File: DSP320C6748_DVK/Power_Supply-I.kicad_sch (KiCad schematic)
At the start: 17 parts, among them IC1 TPS650250RHBR, IC2 TPS3707-33DR, IC3 TPS2087D, IC4 TPS2068DGNR, IC5 SN74AHC1G04DBVR, J1 Barrel_Jack_Switch, J2 USB_B_Mini, U2 NCP-347MTAE

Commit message: TPS650250 Section Added
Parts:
- removed IC1: TPS650250RHBR, TPS650250RHBR:QFN50P500X500X100-33N-D, symbol TPS650250RHBR:TPS650250RHBR
- added D2: PWR_Red, symbol Device:LED_Small
- added R7: 1K, symbol Device:R_Small
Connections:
- net +5V: now also R7.1
- net GND: now also D2.1 (K)
- new net: D2.2 (A), R7.2
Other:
- note added: "Power LED"
- moved on the sheet: IC2, IC3, IC4, IC5, J2, JP1, R6

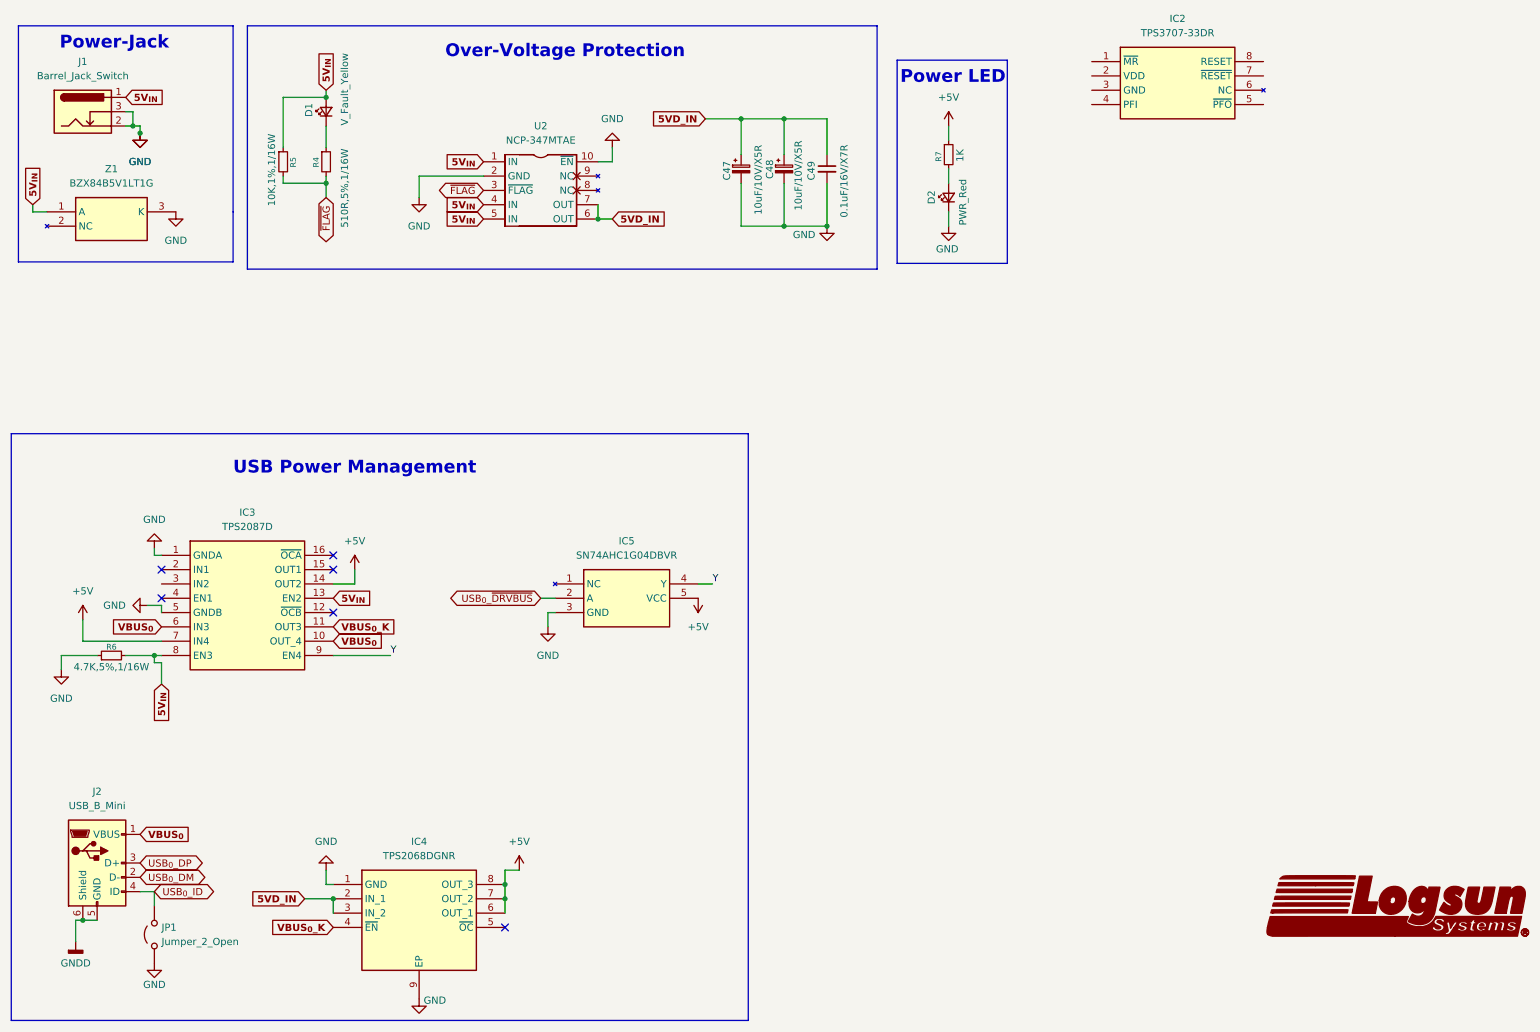
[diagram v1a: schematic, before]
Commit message: POR Generation Section Added
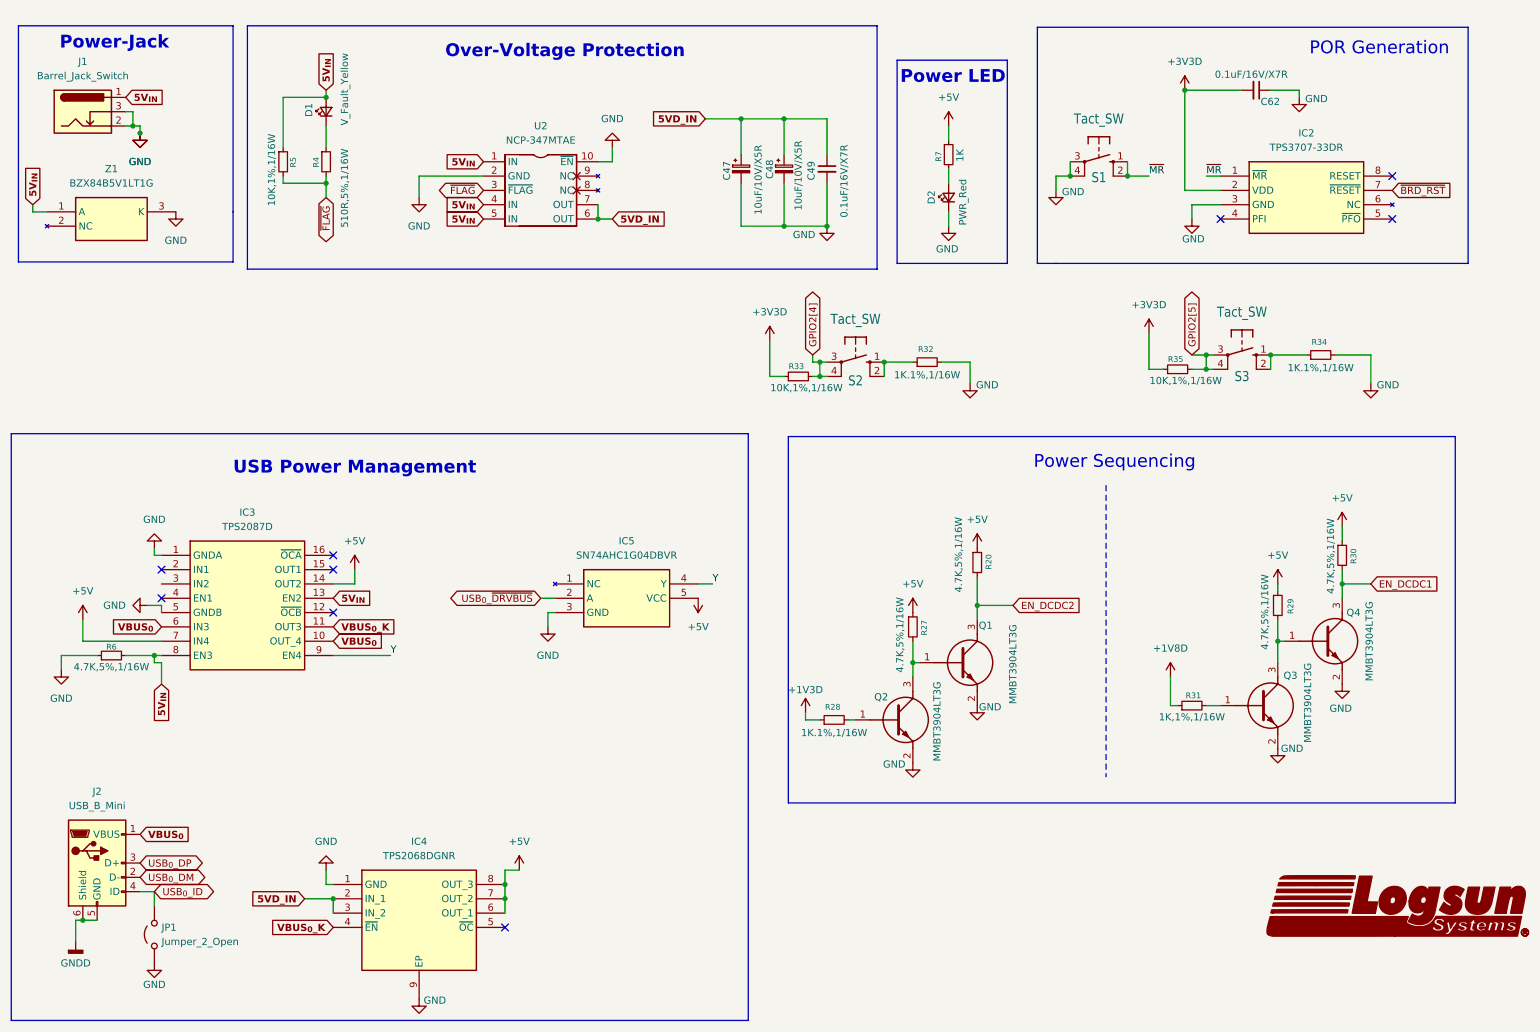
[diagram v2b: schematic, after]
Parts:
- added C62: 0.1uF/16V/X7R, symbol Device:C_Small
- added Q1, Q2, Q3, Q4: MMBT3904LT3G, SOT96P237X111-3N, symbol MMBT3904LT3G:MMBT3904LT3G
- added R20, R27, R29, R30: 4.7K,5%,1/16W, symbol Device:R_Small
- added R28, R32, R34: 1K.1%,1/16W, symbol Device:R_Small
- added R31: 1K,1%,1/16W, symbol Device:R_Small
- added R33, R35: 10K,1%,1/16W, symbol Device:R_Small
- added S1, S2, S3: Tact_SW, LOGSUN:LGS-KC-B3F-10XX, symbol LOGSUN:LGS-KC-10-XX
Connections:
- net +5V: now also R20.1, R27.1, R29.1, R30.1
- net GND: now also IC2.3 (GND), C62.1, Q1.2 (E), Q2.2 (E), Q3.2 (E), Q4.2 (E), R32.2, R34.2, S1.3 (P), S1.4 (P1)
- net ~{MR}: now reaches IC2.1 (~{MR})
- net ~{MR}: now also S1.1 (S), S1.2 (S1)
- net +3V3D: now reaches IC2.2 (VDD)
- net +3V3D: now also C62.2, R33.1, R35.1
- net ~{BRD_RST}: now reaches IC2.7 (~{RESET})
- new net: Q2.1 (B), R28.2
- new net: Q3.3 (C), Q4.1 (B), R29.2
- new net: Q1.1 (B), Q2.3 (C), R27.2
- new net: Q3.1 (B), R31.2
- new net: R34.1, S3.1 (S), S3.2 (S1)
- new net: R32.1, S2.1 (S), S2.2 (S1)
- new net +1V3D: R28.1
- new net +1V8D: R31.1
- new net EN_DCDC1: Q4.3 (C), R30.2
- new net EN_DCDC2: Q1.3 (C), R20.2
- new net GPIO2[4]: R33.2, S2.3 (P), S2.4 (P1)
- new net GPIO2[5]: R35.2, S3.3 (P), S3.4 (P1)
- no-connect marks 6 -> 9
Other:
- note added: "POR Generation"
- note added: "Power Sequencing"
- moved on the sheet: IC2

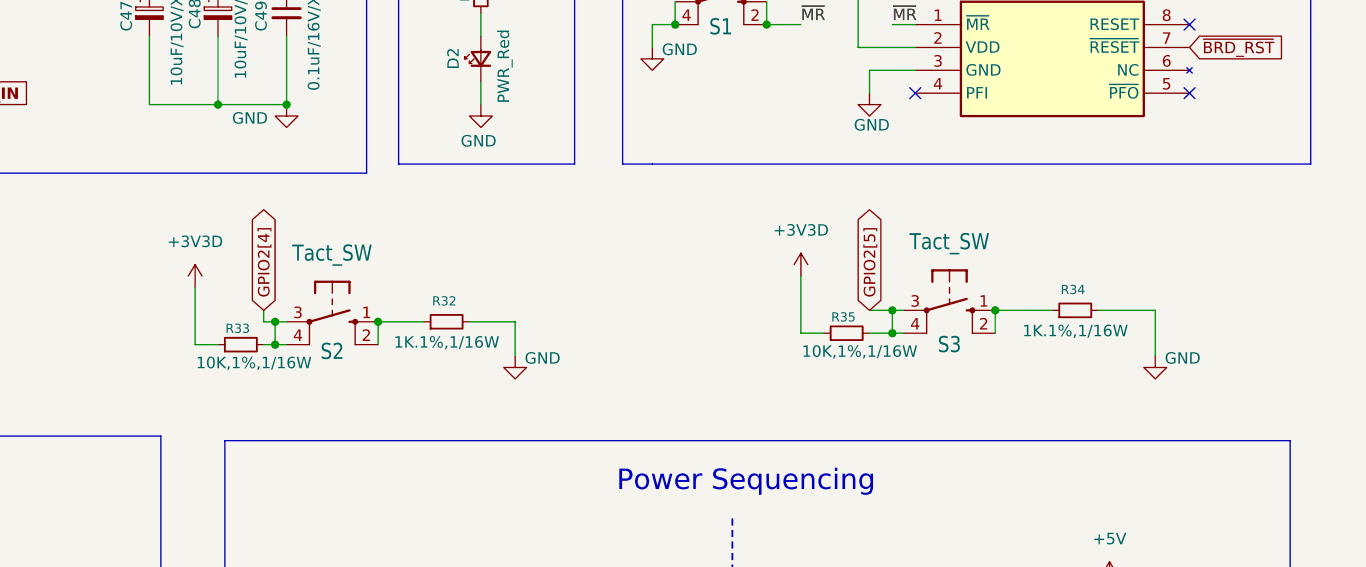
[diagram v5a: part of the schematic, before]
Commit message: Connectors and mislleneous components added
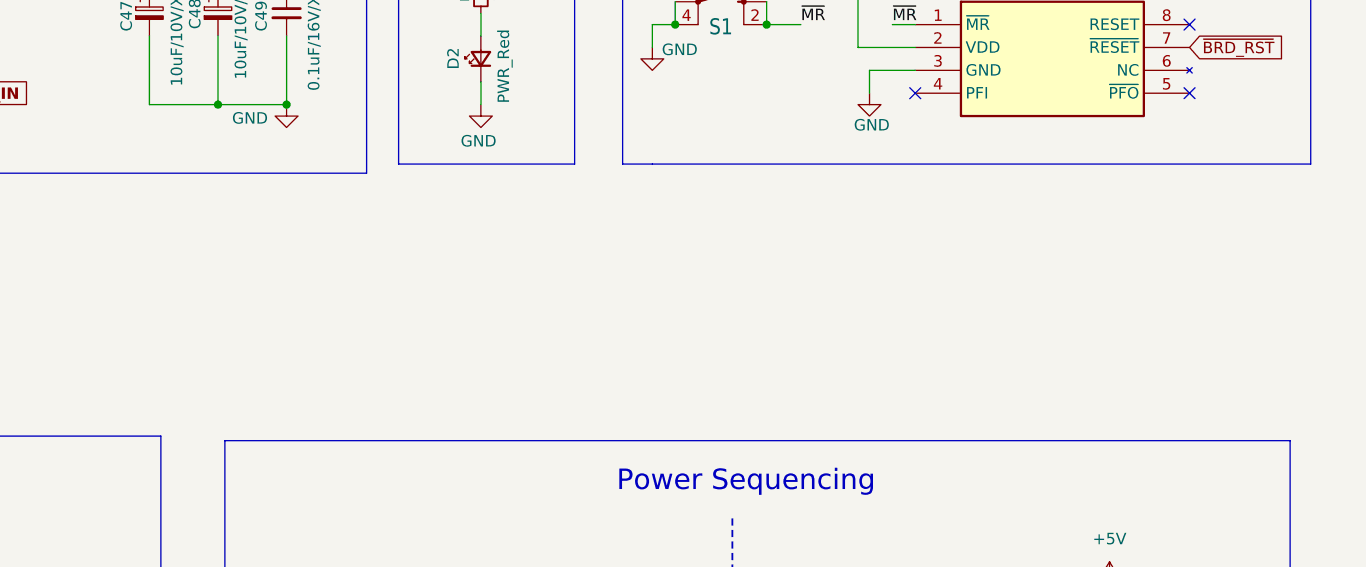
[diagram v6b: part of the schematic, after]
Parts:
- removed R32, R34: 1K.1%,1/16W, symbol Device:R_Small
- removed R33, R35: 10K,1%,1/16W, symbol Device:R_Small
- removed S2, S3: Tact_SW, LOGSUN:LGS-KC-B3F-10XX, symbol LOGSUN:LGS-KC-10-XX

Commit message: Whole Schematic Reannotation Done
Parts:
- renumbered C47 to C54, C48 to C55, C49 to C56, C62 to C57, D1 to D3, D2 to D4, IC3 to IC4, IC4 to IC5, IC5 to IC6, IC2 to IC7, J1 to J3, J2 to J4, Q2 to Q1, Q1 to Q2, R6 to R44, R5 to R45, R4 to R46, R28 to R47, R27 to R48, R7 to R49, R20 to R50, R31 to R51, R29 to R52, R30 to R53

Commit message: Schematic corrections-I
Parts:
- added C203: 0.1uF/16V/X7R, symbol Device:C_Small
- added R263: 4.7K,5%,1/16W, symbol Device:R_Small
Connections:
- net 5VD_IN: now also IC4.13 (EN2), IC4.8 (EN3), R44.2
- net 5V_{IN}: now also Z1.3 (K); no longer IC4.13 (EN2), IC4.8 (EN3), R44.2, Z1.1 (A)
- net GND: now also J4.5 (GND), Z1.1 (A), C203.2, R263.1; no longer Z1.3 (K)
- net GNDD: no longer J4.5 (GND)
- net VBUS_{0}_K: now also IC4.3 (IN2), C203.1, R263.2
